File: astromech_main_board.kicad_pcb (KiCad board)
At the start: 2 copper layers, 100.3 x 109.2 mm, 87 parts, among them IC1 MAX11645EUA+, J1 Screw_Terminal_01x02, J10 Conn_01x05, J11 Conn_01x06, J12 Conn_01x04, J13 Conn_01x05, J14 Conn_01x04, J15 Conn_01x04, J19 Conn_01x04, J2 Screw_Terminal_01x02, J20 Conn_01x04, J21 Conn_01x04, J3 Screw_Terminal_01x02, J4 IO_XPAND, J5 Conn_01x06, J6 Conn_01x06, J7 Conn_01x08, J8 Conn_01x03, J9 Conn_01x06, U1 TCA9554DW, U10 LS7366R, U11 LS7366R, U2 TCA9554DW, U3 NCP1117-3.3_SOT223, U4 NCP1117-5.0_TO252, U5 SC16IS752IPW_128, U6 TXB0108PW, U7 TCA9517ADGK, U8 74HC14, U9 LS7366R, Y1 Crystal, Y2 Crystal

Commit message: renamed nets
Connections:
- net /IO36 renamed /SCR_SPICLK
- net /IO37 renamed /SCR_SPIQ
- net /IO46 renamed /PWM_HEAD
- net /IO47 renamed /PWM_LEFT
- net /IO48 renamed /PWM_RIGHT
- net /IO5 renamed /SPI_CS_LEFT
- net /IO6 renamed /SPI_CS_HEAD
- net /IO7 renamed /SPI_CS_RIGHT

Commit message: compact layout start
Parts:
- C10, C11, C12, R13: moved to F.Cu
- U5: moved to B.Cu
- moved U9 136.0 mm to (96.5, 104.1)
- moved U10 136.0 mm to (96.5, 115.6)
- moved U11 135.9 mm to (96.5, 127.0)
- moved R13 130.9 mm to (102.9, 101.6), turned to 180 degrees
- moved C10 129.6 mm to (102.9, 105.4)
- moved C11 129.6 mm to (102.9, 115.6)
- moved C12 129.6 mm to (102.9, 127.0)
- moved C19 103.1 mm to (86.8, 175.3)
- moved Y2 103.1 mm to (81.7, 170.2)
- moved C18 103.1 mm to (76.4, 175.3)
- moved R22 101.0 mm to (108.3, 167.3)
- moved C15 99.9 mm to (270.4, 8.89)
- moved U5 98.4 mm to (101.3, 161.0)
- moved J21 93.6 mm to (160.0, 85.5), turned to 90 degrees
- moved R19 92.2 mm to (128.9, 147.3), turned to 180 degrees
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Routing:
- net 5V: track 242.0 -> 0.00 mm, vias 7 -> 0
- net /I2C_3V3_SCL: track 164.3 -> 0.00 mm, vias 7 -> 0
- net /I2C_3V3_SDA: track 159.1 -> 0.00 mm, vias 7 -> 0
- net /IO3: track 149.4 -> 0.00 mm, vias 1 -> 0
- net /IO0: track 140.4 -> 0.00 mm, vias 1 -> 0
- net /SCR_SPICLK: track 130.4 -> 0.00 mm, vias 1 -> 0
- net /SCR_SPIQ: track 128.1 -> 0.00 mm, vias 1 -> 0
- net /IO4: track 126.7 -> 0.00 mm, vias 1 -> 0
- net /IO38: track 125.3 -> 0.00 mm, vias 1 -> 0
- net /IO39: track 122.5 -> 0.00 mm, vias 1 -> 0
- net /IO2: track 117.7 -> 0.00 mm, vias 1 -> 0
- net /IO1: track 115.1 -> 0.00 mm, vias 1 -> 0
- net /ENC_CNT_EN: track 112.9 -> 0.00 mm, vias 4 -> 0
- net /ENC_INT: track 111.4 -> 0.00 mm, vias 4 -> 0
- net /IO10: track 97.0 -> 0.00 mm, vias 1 -> 0
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- removed copper zone on F.Cu, net /3V3_IN
- removed copper zone on F.Cu, net /5V_IN
- removed copper zone on F.Cu, net Net-(J1-Pin_1)
- removed copper zone on F.Cu, net Net-(J2-Pin_1)
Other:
- board size 100.3 x 109.2 mm -> 70 x 88.9 mm

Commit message: implemented suggestions
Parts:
- removed C4, C5, C6: C_Small, Capacitor_SMD:C_1206_3216Metric
- removed J12: Conn_01x04, astromech_footprints:691210910004
- removed J2, J3: Screw_Terminal_01x02, astromech_footprints:PHOENIX_1984617
- removed R17: R_Small_US, Resistor_SMD:R_1206_3216Metric
- removed U1, U2: TCA9554DW, Package_SO:SOIC-16W_7.5x10.3mm_P1.27mm
- added J18: Screw_Terminal_01x10, astromech_footprints:PHOENIX_1984691, F.Cu at (199.9, 62.0)
- added R7: ~, Resistor_SMD:R_1206_3216Metric, F.Cu at (125.5, 87.6)
- J1: value Screw_Terminal_01x02 -> Conn_01x06; footprint astromech_footprints:PHOENIX_1984617 -> Connector_PinHeader_2.54mm:PinHeader_2x03_P2.54mm_Vertical
- R8: value R_Small_US -> ~
- U6: value TXB0108PW -> PCF8575PWR; footprint Package_SO:TSSOP-20_4.4x6.5mm_P0.65mm -> astromech_footprints:SOP65P640X120-24N
- Y1: footprint Crystal:Crystal_SMD_HC49-SD_HandSoldering -> Crystal:Crystal_SMD_Abracon_ABM3-2Pin_5.0x3.2mm
- Y2: footprint Crystal:Crystal_SMD_HC49-SD_HandSoldering -> Crystal:Crystal_HC49-U_Vertical
- moved J1 51.0 mm to (117.9, 88.3)
- moved J10 37.6 mm to (160.0, 73.0), turned to 90 degrees
- moved J11 15.9 mm to (205.1, 64.1), turned to 0 degrees
- moved J9 6.38 mm to (214.6, 64.1)
- moved H2 6.35 mm to (223.5, 66.0)
- moved H4 6.35 mm to (223.5, 142.2)
- moved J13 6.35 mm to (223.0, 85.9)
- moved J5 6.35 mm to (223.0, 113.3)
- moved J6 6.35 mm to (223.0, 130.2)
- moved H1 3.81 mm to (160.0, 62.2)
- moved J15 0.64 mm to (160.0, 121.5)
- moved J20 0.64 mm to (160.0, 97.9)
- moved C2 0.63 mm to (195.6, 75.6)
- moved J14 0.63 mm to (160.0, 133.3)
- moved J19 0.63 mm to (160.0, 109.7)
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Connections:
- D1 pad 1: GND -> Net-(D1-K)
- D2 pad 1: GND -> Net-(D2-K)
- D3 pad 1: GND -> Net-(D3-K)
- D4 pad 1: GND -> Net-(D4-K)
- F1 pad 1: Net-(J1-Pin_1) -> Net-(J18-Pin_10)
- J1 pad 2: GND -> Net-(J1-Pin_2)
- J14 pad 2: /UART_TXA -> /IOTX
- J14 pad 3: /UART_RXA -> /IORX
- J15 pad 1: 3V3 -> /UART_TXA
- J15 pad 2: /UART_TXB -> /UART_RXA
- J15 pad 3: /UART_RXB -> /UART_TXB
- J15 pad 4: GND -> /UART_RXB
- J4 pad 1: Net-(J4-Pin_1) -> Net-(D1-K)
- J4 pad 2: Net-(J4-Pin_2) -> Net-(D2-K)
- J4 pad 3: Net-(J4-Pin_3) -> Net-(D3-K)
- J4 pad 4: Net-(J4-Pin_4) -> Net-(D4-K)
- R14 pad 1: Net-(J4-Pin_4) -> 3V3
- R14 pad 2: Net-(D4-A) -> Net-(D1-A)
- R15 pad 1: Net-(J4-Pin_3) -> 3V3
- R15 pad 2: Net-(D3-A) -> Net-(D2-A)
- R16 pad 2: Net-(J12-Pin_1) -> Net-(J1-Pin_1)
- R18 pad 1: Net-(J4-Pin_2) -> 3V3
- R18 pad 2: Net-(D2-A) -> Net-(D3-A)
- R19 pad 1: Net-(J4-Pin_1) -> 3V3
- R19 pad 2: Net-(D1-A) -> Net-(D4-A)
- R3 pad 2: /IO10 -> /IO_INT
- R4 pad 1: 3V3 -> /IO42
- R4 pad 2: /IO9 -> Net-(J1-Pin_2)
- R8 pad 1: 3V3 -> Net-(JP13-C)
- R8 pad 2: Net-(U6-OE) -> GND
- U10 pad 13: /ENC_CNT_EN -> unconnected-(U10-CNT_EN-Pad13)
- U10 pad 7: /IO13 -> /SPI_COPI
- U11 pad 13: /ENC_CNT_EN -> unconnected-(U11-CNT_EN-Pad13)
- U11 pad 7: /IO13 -> /SPI_COPI
- U13 pad 15: /IO9 -> /IO_INT
- U13 pad 25: /ENC_CNT_EN -> /IO19
- U6 pad 1: Net-(JP13-C) -> /IO_INT
- U6 pad 10: Net-(U6-OE) -> Net-(J4-Pin_7)
- U6 pad 11: GND -> Net-(J4-Pin_8)
- U6 pad 12: unconnected-(U6-B8-Pad12) -> GND
- U6 pad 13: unconnected-(U6-B7-Pad13) -> Net-(J4-Pin_9)
- U6 pad 14: unconnected-(U6-B6-Pad14) -> Net-(J4-Pin_10)
- U6 pad 15: unconnected-(U6-B5-Pad15) -> Net-(J4-Pin_11)
- U6 pad 16: unconnected-(U6-B4-Pad16) -> Net-(J4-Pin_12)
- U6 pad 17: unconnected-(U6-B3-Pad17) -> Net-(J4-Pin_13)
- U6 pad 18: unconnected-(U6-B2-Pad18) -> Net-(J4-Pin_14)
- U6 pad 19: 5V -> Net-(J4-Pin_15)
- U6 pad 2: 3V3 -> GND
- U6 pad 20: /RC_UART_5V -> Net-(J4-Pin_16)
- U6 pad 3: unconnected-(U6-A2-Pad3) -> GND
- U6 pad 4: unconnected-(U6-A3-Pad4) -> Net-(D1-K)
- U6 pad 5: unconnected-(U6-A4-Pad5) -> Net-(D2-K)
- U6 pad 6: unconnected-(U6-A5-Pad6) -> Net-(D3-K)
- U6 pad 7: unconnected-(U6-A6-Pad7) -> Net-(D4-K)
- U6 pad 8: unconnected-(U6-A7-Pad8) -> Net-(J4-Pin_5)
- U6 pad 9: unconnected-(U6-A8-Pad9) -> Net-(J4-Pin_6)
- U9 pad 13: /ENC_CNT_EN -> unconnected-(U9-CNT_EN-Pad13)
- U9 pad 7: /IO13 -> /SPI_COPI
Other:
- board size 70 x 88.9 mm -> 76.2 x 88.9 mm

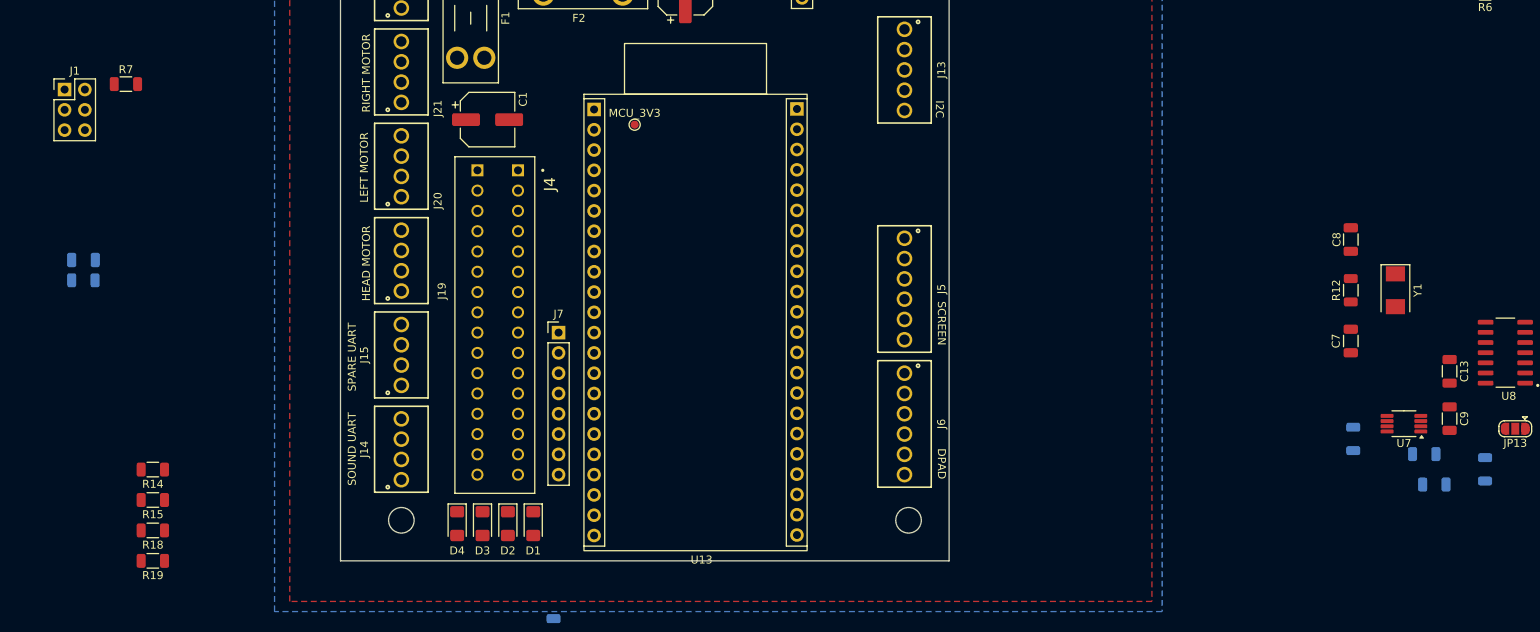
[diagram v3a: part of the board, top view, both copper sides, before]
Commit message: added values, 2N7002, and updated unused pins
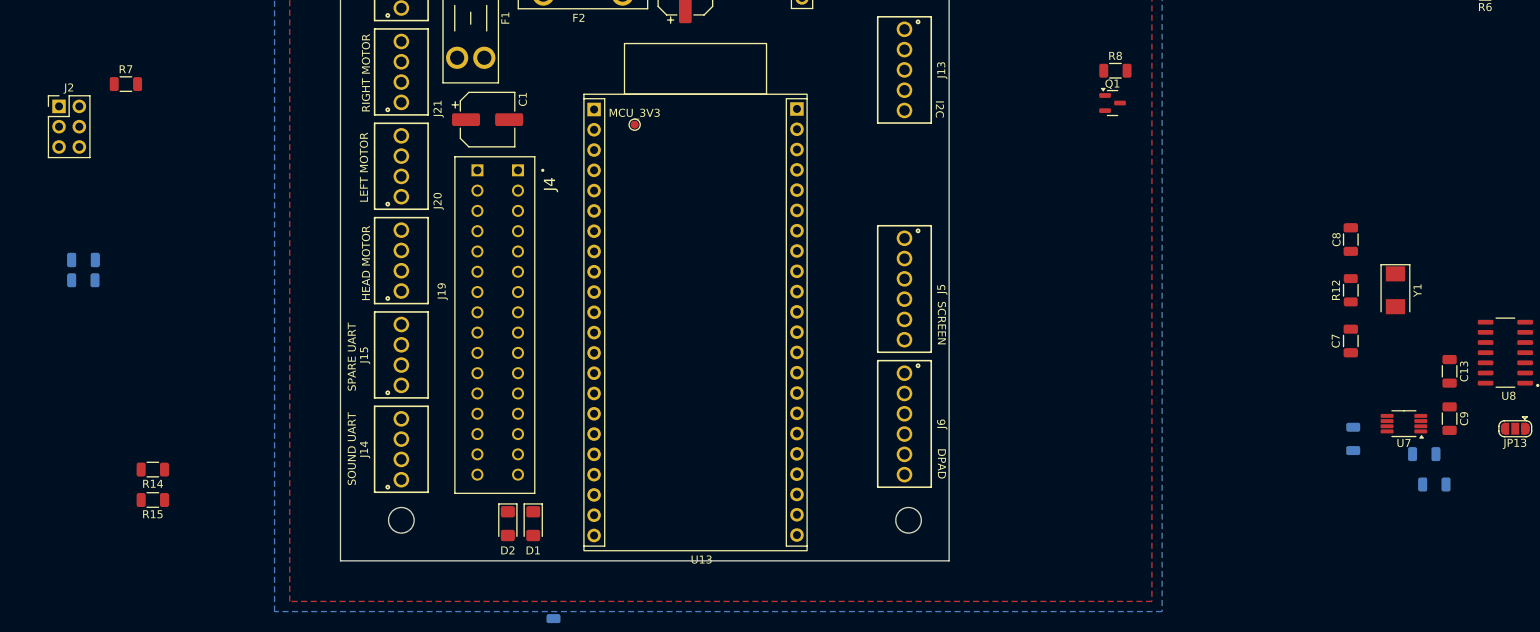
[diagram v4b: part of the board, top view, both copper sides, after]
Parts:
- removed D3, D4: LED, LED_SMD:LED_1206_3216Metric_Pad1.42x1.75mm_HandSolder
- removed J1: Conn_01x06, Connector_PinHeader_2.54mm:PinHeader_2x03_P2.54mm_Vertical
- removed J7: Conn_01x08, Connector_PinHeader_2.54mm:PinHeader_1x08_P2.54mm_Vertical
- removed R18, R19: R_Small_US, Resistor_SMD:R_1206_3216Metric
- added J2: Conn_02x03_Odd_Even, Connector_PinHeader_2.54mm:PinHeader_2x03_P2.54mm_Vertical, F.Cu at (117.2, 90.4)
- added Q1: 2N7002, Package_TO_SOT_SMD:SOT-23, F.Cu at (249.1, 90.0)
- C1, C2: value 0.1u -> 100uF
- C10, C11, C12, C13, C16, C3, C9: value C_Small -> .1uF
- C14, C15: value C_Small -> 10uF
- C17: value C_Small -> 1uF
- R10, R5, R6, R9: value R_Small_US -> 4.7K
- R11, R13, R20, R21, R22, R3: value R_Small_US -> 10K
- R14, R15: value R_Small_US -> 2K
- R16, R4: value R_Small_US -> 1K
- R7: value ~ -> 1K
- R8: value ~ -> 4.7K; moved to F.Cu
- Y1: value Crystal -> 8MHz
- moved R8 68.1 mm to (249.4, 86.0), turned to 0 degrees
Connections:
- J4 pad 10: Net-(J4-Pin_10) -> /IO10
- J4 pad 11: Net-(J4-Pin_11) -> /IO17
- J4 pad 12: Net-(J4-Pin_12) -> /IO19
- J4 pad 13: Net-(J4-Pin_13) -> /IO21
- J4 pad 14: Net-(J4-Pin_14) -> /IO35
- J4 pad 15: Net-(J4-Pin_15) -> /IO40
- J4 pad 16: Net-(J4-Pin_16) -> /IO45
- J4 pad 9: Net-(J4-Pin_9) -> /IO8
- R7 pad 2: Net-(JP13-C) -> Net-(Q1-G)
- R8 pad 1: Net-(JP13-C) -> +3.3V
- R8 pad 2: GND -> Net-(JP13-C)
- U10 pad 7: /SPI_COPI -> /IO13
- U11 pad 7: /SPI_COPI -> /IO13
- U5 pad 13: /I2C_3V3_SDA -> /I2C_3V3_SCL
- U5 pad 14: /I2C_3V3_SCL -> /I2C_3V3_SDA
- U6 pad 13: Net-(J4-Pin_9) -> unconnected-(U6-P10-Pad13)
- U6 pad 14: Net-(J4-Pin_10) -> unconnected-(U6-P11-Pad14)
- U6 pad 15: Net-(J4-Pin_11) -> unconnected-(U6-P12-Pad15)
- U6 pad 16: Net-(J4-Pin_12) -> unconnected-(U6-P13-Pad16)
- U6 pad 17: Net-(J4-Pin_13) -> unconnected-(U6-P14-Pad17)
- U6 pad 18: Net-(J4-Pin_14) -> unconnected-(U6-P15-Pad18)
- U6 pad 19: Net-(J4-Pin_15) -> unconnected-(U6-P16-Pad19)
- U6 pad 20: Net-(J4-Pin_16) -> unconnected-(U6-P17-Pad20)
- U9 pad 7: /SPI_COPI -> /IO13

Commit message: switch qwiic pinout order
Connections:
- J11 pad 1: /SCL_BUFD -> GND
- J11 pad 2: /SDA_BUFD -> 3V3
- J11 pad 3: 3V3 -> /SDA_BUFD
- J11 pad 4: GND -> /SCL_BUFD
- J9 pad 1: /SCL_BUFD -> GND
- J9 pad 2: /SDA_BUFD -> 3V3
- J9 pad 3: 3V3 -> /SDA_BUFD
- J9 pad 4: GND -> /SCL_BUFD
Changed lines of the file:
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@@
 			(size 0.6604 1.5494)
 			(layers "F.Cu" "F.Paste" "F.Mask")
-			(net 44 "/SCL_BUFD")
+			(net 2 "GND")
 			(pinfunction "Pin_1")
 			(pintype "passive")
@@
 			(size 0.6604 1.5494)
 			(layers "F.Cu" "F.Paste" "F.Mask")
-			(net 45 "/SDA_BUFD")
+			(net 4 "3V3")
 			(pinfunction "Pin_2")
 			(pintype "passive")
@@
 			(size 0.6604 1.5494)
 			(layers "F.Cu" "F.Paste" "F.Mask")
-			(net 4 "3V3")
+			(net 45 "/SDA_BUFD")
 			(pinfunction "Pin_3")
 			(pintype "passive")
@@
 			(size 0.6604 1.5494)
 			(layers "F.Cu" "F.Paste" "F.Mask")
-			(net 2 "GND")
+			(net 44 "/SCL_BUFD")
 			(pinfunction "Pin_4")
 			(pintype "passive")
@@
 			(size 0.6604 1.5494)
 			(layers "F.Cu" "F.Paste" "F.Mask")
-			(net 44 "/SCL_BUFD")
+			(net 2 "GND")
 			(pinfunction "Pin_1")
 			(pintype "passive")
@@
 			(size 0.6604 1.5494)
 			(layers "F.Cu" "F.Paste" "F.Mask")
-			(net 45 "/SDA_BUFD")
+			(net 4 "3V3")
 			(pinfunction "Pin_2")
 			(pintype "passive")
@@
 			(size 0.6604 1.5494)
 			(layers "F.Cu" "F.Paste" "F.Mask")
-			(net 4 "3V3")
+			(net 45 "/SDA_BUFD")
 			(pinfunction "Pin_3")
 			(pintype "passive")
@@
 			(size 0.6604 1.5494)
 			(layers "F.Cu" "F.Paste" "F.Mask")
-			(net 2 "GND")
+			(net 44 "/SCL_BUFD")
 			(pinfunction "Pin_4")
 			(pintype "passive")

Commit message: schematic updates
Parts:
- removed J13: Conn_01x05, astromech_footprints:691210910005
- removed J14: Conn_01x04, astromech_footprints:691210910004
- removed J5, J6: Conn_01x06, astromech_footprints:691210910006
- added J1: Conn_01x03, astromech_footprints:691210910003, F.Cu at (56.5, 63.0)
- added J3: Conn_01x03, astromech_footprints:691210910003, F.Cu at (56.5, 71.2)
- added J7: Conn_01x03, astromech_footprints:691210910003, F.Cu at (56.5, 79.4)
- added P15: TestPoint, TestPoint:TestPoint_Pad_D1.0mm, F.Cu at (62.9, 60.4)
- added P16: TestPoint, TestPoint:TestPoint_Pad_D1.0mm, F.Cu at (62.9, 63.5)
- added P17: TestPoint, TestPoint:TestPoint_Pad_D1.0mm, F.Cu at (62.9, 66.5)
- J10: value Conn_01x05 -> 61201621621; footprint astromech_footprints:691210910005 -> astromech_footprints:61201621621
- moved J10 73.0 mm to (93.3, 43.2)
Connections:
- J10 pad 1: 5V -> /TOUCH_X-
- J10 pad 2: 3V3 -> /TOUCH_Y-
- J10 pad 3: /SCL_BUFD -> /TOUCH_X+
- J10 pad 4: /SDA_BUFD -> /TOUCH_Y+
- J10 pad 5: GND -> /SCR_D/C
- J4 pad 10: /IO10 -> Net-(J4-Pin_10)
- J4 pad 11: /IO17 -> Net-(J4-Pin_11)
- J4 pad 12: /IO19 -> Net-(J4-Pin_12)
- J4 pad 13: /IO21 -> Net-(J4-Pin_13)
- J4 pad 14: /IO35 -> /IO8
- J4 pad 9: /IO8 -> Net-(J4-Pin_9)
- U13 pad 10: /IO17 -> /TOUCH_Y+
- U13 pad 16: /IO10 -> /TOUCH_X+
- U13 pad 25: /IO19 -> /TOUCH_X-
- U13 pad 27: /IO21 -> /TOUCH_Y-
- U13 pad 32: /IO35 -> /SCR_D/C
- U6 pad 13: unconnected-(U6-P10-Pad13) -> Net-(J4-Pin_9)
- U6 pad 14: unconnected-(U6-P11-Pad14) -> Net-(J4-Pin_10)
- U6 pad 15: unconnected-(U6-P12-Pad15) -> Net-(J4-Pin_11)
- U6 pad 16: unconnected-(U6-P13-Pad16) -> Net-(J4-Pin_12)
- U6 pad 17: unconnected-(U6-P14-Pad17) -> Net-(J4-Pin_13)
- U6 pad 18: unconnected-(U6-P15-Pad18) -> Net-(U6-P15)
- U6 pad 19: unconnected-(U6-P16-Pad19) -> Net-(U6-P16)
- U6 pad 20: unconnected-(U6-P17-Pad20) -> Net-(U6-P17)

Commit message: new layout
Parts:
- removed P15, P16, P17: TestPoint, TestPoint:TestPoint_Pad_D1.0mm
- C10, C11, C12, C17, C18, C19, C7, C8, JP7, JP8, R1, R12, R14, R15, R2, U10, U11, U9, Y1: moved to B.Cu
- C3, R10, R11, R20, R21, R22, R3, R9, U5, U6: moved to F.Cu
- moved J3 168.2 mm to (223.5, 91.4), turned to 90 degrees
- moved J1 168.1 mm to (223.5, 81.9), turned to 90 degrees
- moved JP8 152.8 mm to (114.3, 25.4)
- moved J10 151.9 mm to (222.3, 123.4)
- moved JP7 147.9 mm to (114.9, 62.2)
- moved U4 147.7 mm to (121.2, 25.7)
- moved C15 146.6 mm to (124.9, 27.3)
- moved C14 138.1 mm to (121.3, 62.0)
- moved U6 127.7 mm to (181.9, 111.8), turned to 180 degrees
- moved J7 115.6 mm to (160.0, 130.8), turned to 90 degrees
- moved R13 112.3 mm to (209.4, 137.2)
- moved C18 110.9 mm to (183.1, 144.8)
- moved R5 109.8 mm to (193.2, 111.8)
- moved R6 107.7 mm to (193.2, 109.2)
- moved J2 103.8 mm to (220.3, 101.6), turned to 90 degrees
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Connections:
- R8 pad 1: +3.3V -> 3V3
- U6 pad 18: Net-(U6-P15) -> unconnected-(U6-P15-Pad18)
- U6 pad 19: Net-(U6-P16) -> unconnected-(U6-P16-Pad19)
- U6 pad 20: Net-(U6-P17) -> unconnected-(U6-P17-Pad20)
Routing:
- net /SCL_BUFD: track 0.00 -> 13.1 mm
- net /SDA_BUFD: track 0.00 -> 12.1 mm
- removed copper zone on F.Cu, net 5V

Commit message: new layout done
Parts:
- moved C16 100.3 mm to (174.0, 86.4), turned to 180 degrees
- moved IC1 99.5 mm to (173.7, 91.9)
- moved R1 98.1 mm to (175.5, 81.8)
- moved R2 97.6 mm to (172.5, 81.8)
- moved C15 96.9 mm to (184.8, 103.5), turned to -90 degrees
- moved C17 96.3 mm to (168.5, 86.4), turned to 0 degrees
- moved U4 95.9 mm to (179.4, 101.9), turned to -90 degrees
- moved JP8 95.5 mm to (183.9, 90.8), turned to -90 degrees
- moved C14 77.6 mm to (194.6, 87.4), turned to 180 degrees
- moved U3 76.3 mm to (192.9, 81.8), turned to 0 degrees
- moved JP7 71.6 mm to (183.9, 81.3), turned to 90 degrees
- moved C10 16.1 mm to (177.2, 134.4)
- moved C12 15.8 mm to (177.2, 113.8)
- moved U10 12.5 mm to (182.3, 122.9)
- moved C11 12.5 mm to (177.2, 120.6)
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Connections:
- U13 pad 8: /I2C_3V3_SDA -> /I2C_3V3_SCL
- U13 pad 9: /I2C_3V3_SCL -> /I2C_3V3_SDA
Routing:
- net 5V: track 0.00 -> 42.3 mm
- net /SDA_BUFD: track 12.1 -> 49.9 mm, vias 0 -> 2
- net /SCL_BUFD: track 13.1 -> 46.6 mm
- net Net-(D1-K): track 0.00 -> 29.6 mm, vias 0 -> 4
- net 3V3: track 0.00 -> 28.9 mm, vias 0 -> 6
- net Net-(D2-K): track 0.00 -> 26.3 mm, vias 0 -> 1
- net Net-(J4-Pin_3): track 0.00 -> 24.4 mm, vias 0 -> 1
- net Net-(J4-Pin_4): track 0.00 -> 22.5 mm
- net Net-(J4-Pin_5): track 0.00 -> 21.5 mm
- net Net-(IC1-AIN0): track 0.00 -> 20.9 mm
- net Net-(J18-Pin_8): track 0.00 -> 20.9 mm
- net Net-(J4-Pin_8): track 0.00 -> 20.8 mm
- net Net-(J4-Pin_6): track 0.00 -> 20.7 mm
- net Net-(J4-Pin_7): track 0.00 -> 20.0 mm
- net /3V3_IN: track 0.00 -> 17.1 mm
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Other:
- board size 76.2 x 88.9 mm -> 71.6 x 78 mm
- board text added: "GND"
